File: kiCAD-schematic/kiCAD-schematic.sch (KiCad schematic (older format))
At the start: 34 parts, among them J1 ext. power, J2 keyboard (usb-a), J3 keyboard (ps/2), Q1 2N3904, Q2 2N3906, Q3 2N3904, SW1 ~RESET, SW2 POWER

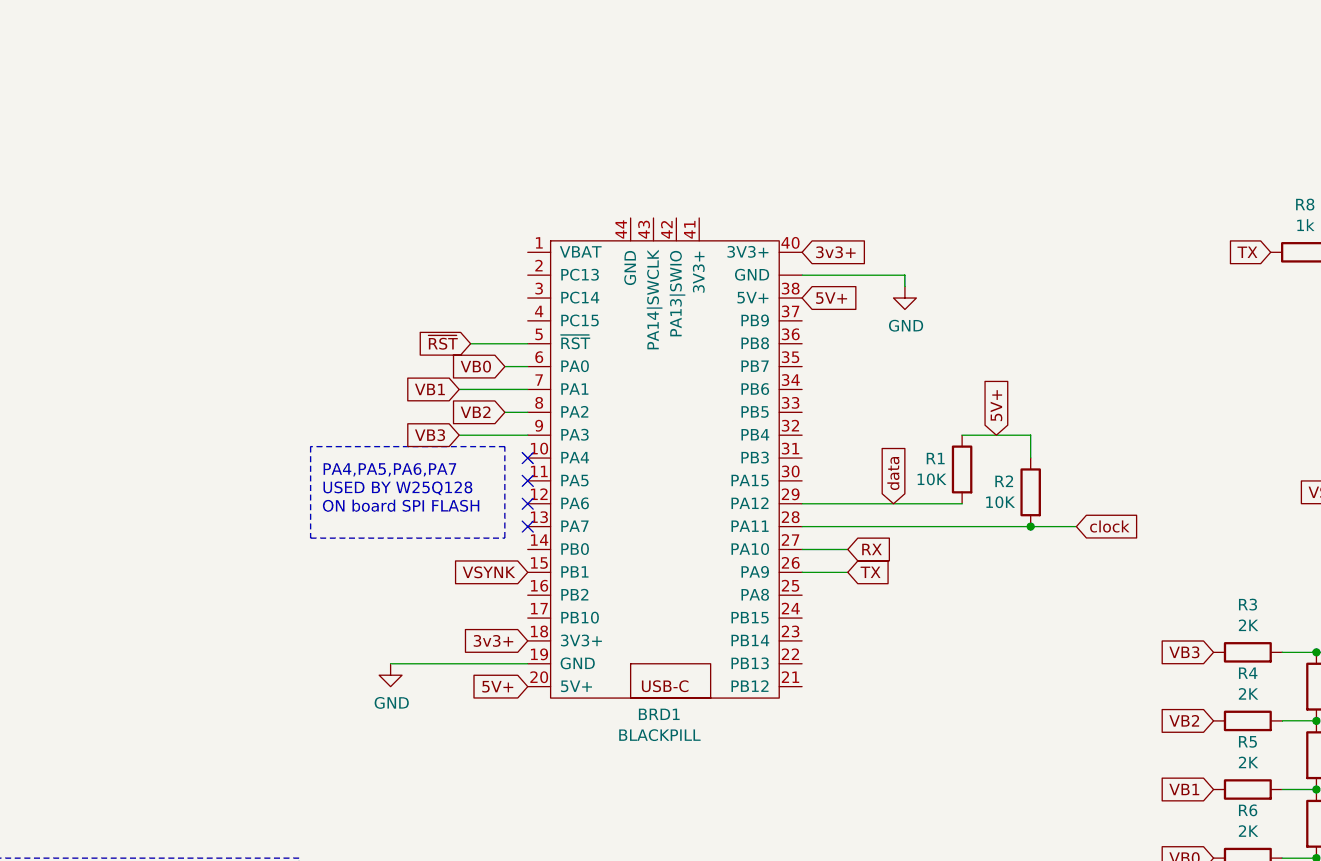
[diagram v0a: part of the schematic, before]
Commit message: travail sur spi-flash WR-BLK ne fonctionne pas écriture erronnée
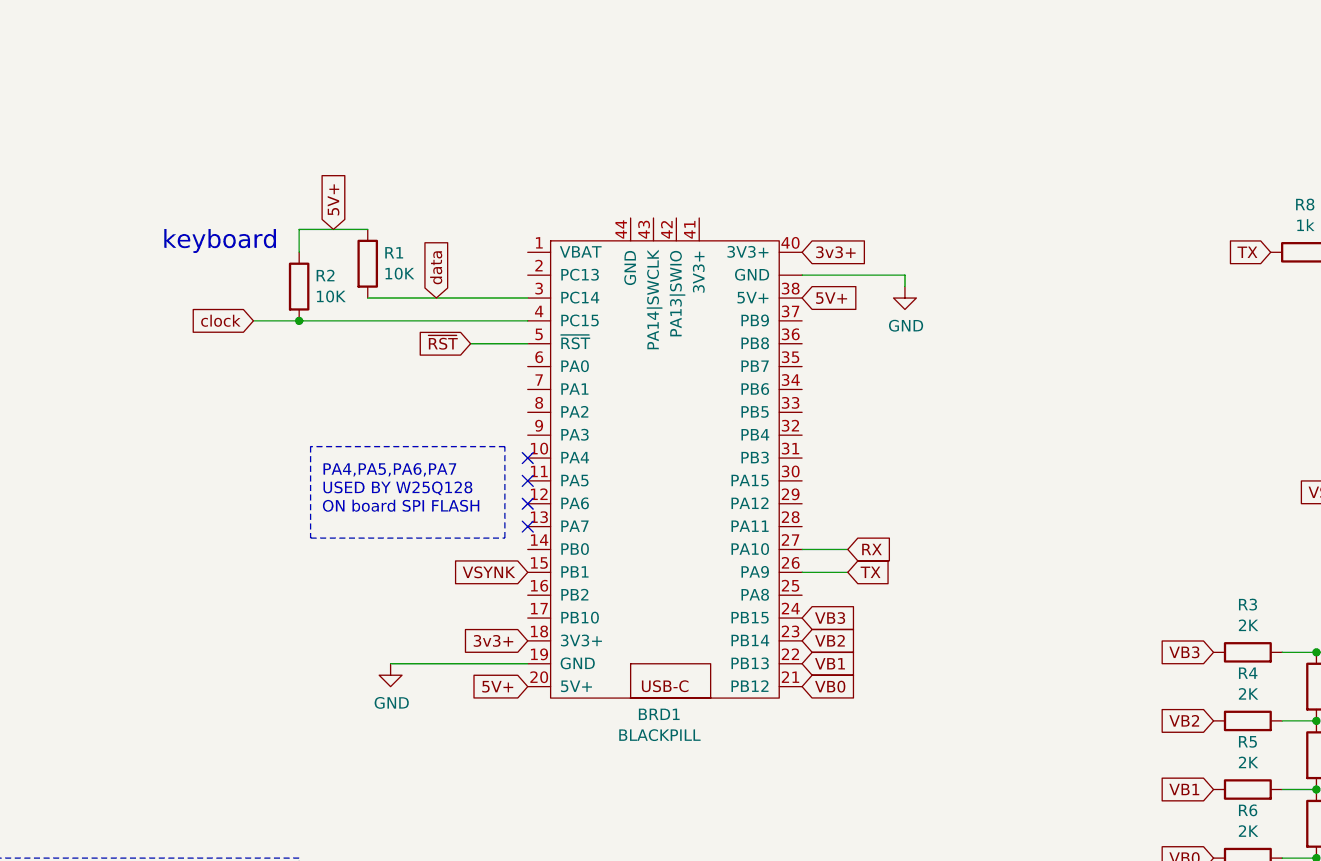
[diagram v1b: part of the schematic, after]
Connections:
- net VB0: now also BRD1.21 (PB12); no longer BRD1.6 (PA0)
- net VB1: now also BRD1.22 (PB13); no longer BRD1.7 (PA1)
- net VB2: now also BRD1.23 (PB14); no longer BRD1.8 (PA2)
- net VB3: now also BRD1.24 (PB15); no longer BRD1.9 (PA3)
- net clock: now also BRD1.4 (PC15); no longer BRD1.28 (PA11)
- net data: now also BRD1.3 (PC14); no longer BRD1.29 (PA12)
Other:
- note added: "keyboard\n"
- moved on the sheet: R1, R2
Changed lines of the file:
@@
 Text GLabel 8250 5500 0    50   Input ~ 0
 VB0
-Text GLabel 5150 3350 0    50   Input ~ 0
+Text GLabel 6450 4750 2    50   Input ~ 0
 VB0
-Wire Wire Line
-	5150 3350 5250 3350
-Text GLabel 4950 3450 0    50   Input ~ 0
+Text GLabel 6450 4650 2    50   Input ~ 0
 VB1
-Wire Wire Line
-	4950 3450 5250 3450
-Text GLabel 5150 3550 0    50   Input ~ 0
+Text GLabel 6450 4550 2    50   Input ~ 0
 VB2
-Wire Wire Line
-	5150 3550 5250 3550
-Text GLabel 4950 3650 0    50   Input ~ 0
+Text GLabel 6450 4450 2    50   Input ~ 0
 VB3
-Wire Wire Line
-	4950 3650 5250 3650
 $Comp
 L Device:R R1
 U 1 1 6002405D
-P 7150 3800
-F 0 "R1" H 7220 3846 50  0000 L CNN
-F 1 "10K" H 7220 3755 50  0000 L CNN
-F 2 "" V 7080 3800 50  0001 C CNN
-F 3 "~" H 7150 3800 50  0001 C CNN
-	1    7150 3800
-	-1   0    0    -1
+P 4550 2900
+F 0 "R1" H 4620 2946 50  0000 L CNN
+F 1 "10K" H 4620 2855 50  0000 L CNN
+F 2 "" V 4480 2900 50  0001 C CNN
+F 3 "~" H 4550 2900 50  0001 C CNN
+	1    4550 2900
+	1    0    0    -1
 $EndComp
 $Comp
 L Device:R R2
 U 1 1 600245BA
-P 7450 3900
-F 0 "R2" H 7520 3946 50  0000 L CNN
-F 1 "10K" H 7520 3855 50  0000 L CNN
-F 2 "" V 7380 3900 50  0001 C CNN
-F 3 "~" H 7450 3900 50  0001 C CNN
-	1    7450 3900
-	-1   0    0    -1
-$EndComp
-Wire Wire Line
-	7450 4050 6450 4050
-Wire Wire Line
-	7150 3950 6450 3950
-Wire Wire Line
-	7450 3750 7450 3650
-Wire Wire Line
-	7450 3650 7150 3650
-Text GLabel 7300 3650 1    50   Input ~ 0
+P 4250 3000
+F 0 "R2" H 4320 3046 50  0000 L CNN
+F 1 "10K" H 4320 2955 50  0000 L CNN
+F 2 "" V 4180 3000 50  0001 C CNN
+F 3 "~" H 4250 3000 50  0001 C CNN
+	1    4250 3000
+	1    0    0    -1
+$EndComp
+Wire Wire Line
+	4250 3150 5250 3150
+Wire Wire Line
+	4550 3050 5250 3050
+Wire Wire Line
+	4250 2850 4250 2750
+Wire Wire Line
+	4250 2750 4550 2750
+Text GLabel 4400 2750 1    50   Input ~ 0
 5V+
-Text GLabel 7650 4050 2    50   Input ~ 0
+Text GLabel 4050 3150 0    50   Input ~ 0
 clock
 Wire Wire Line
-	7650 4050 7450 4050
-Connection ~ 7450 4050
-Text GLabel 6850 3950 1    50   Input ~ 0
+	4050 3150 4250 3150
+Connection ~ 4250 3150
+Text GLabel 4850 3050 1    50   Input ~ 0
 data
 Text GLabel 6450 2850 2    50   Input ~ 0
@@
 	1    0    0    -1
 $EndComp
+Text Notes 3650 2850 0    79   ~ 0
+keyboard\n
 $EndSCHEMATC
